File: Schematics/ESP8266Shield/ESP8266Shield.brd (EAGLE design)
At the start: 49.2 x 48.3 mm, 23 parts, among them IC1 MEGA8-P, Q1 2N5088, Q2 2N5088

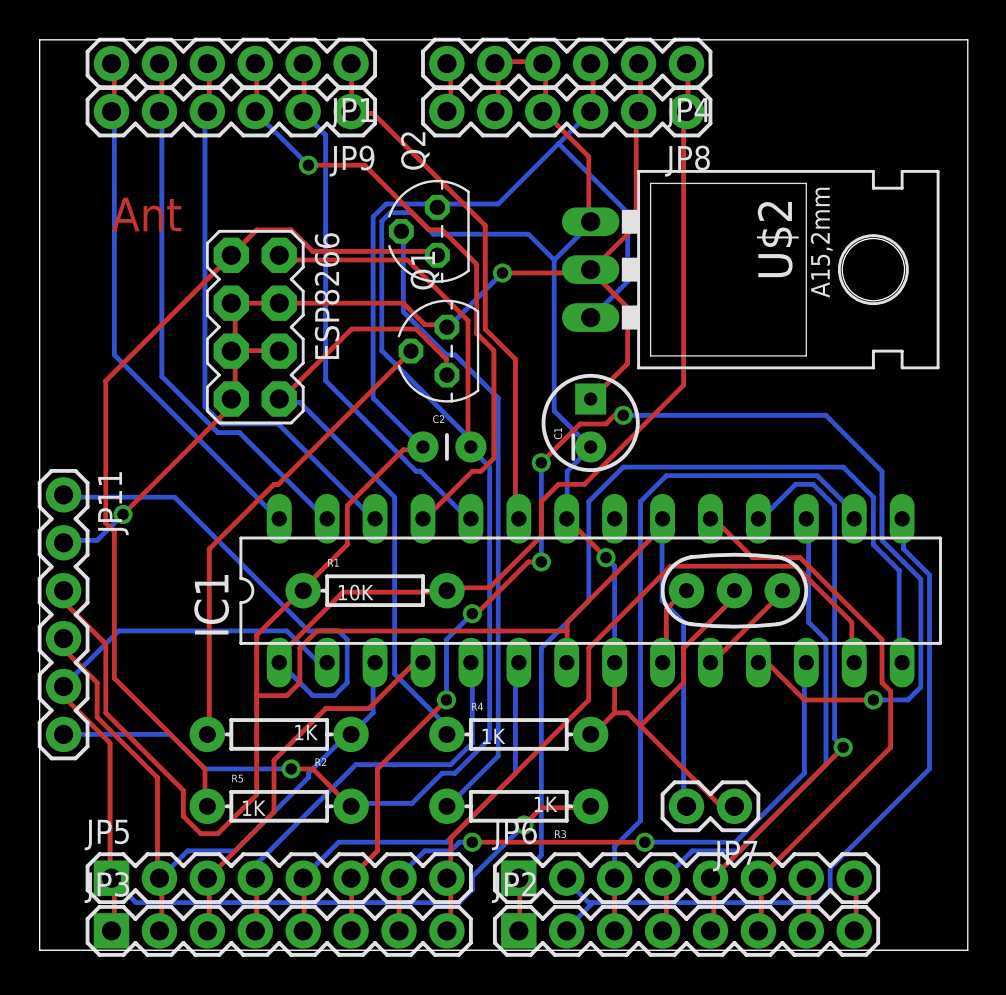
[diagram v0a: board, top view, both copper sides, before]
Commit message: v0.08
Updated Android project to close socket on exit
Updated Arduino projects
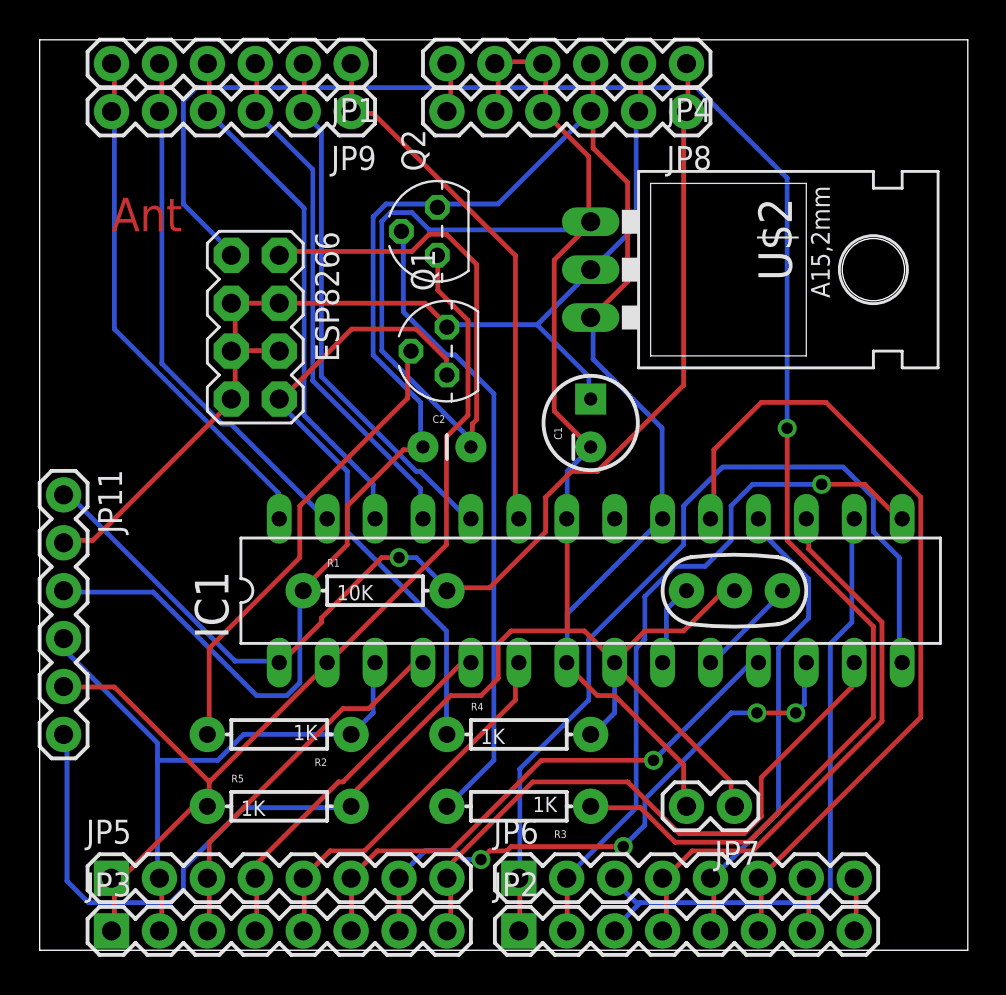
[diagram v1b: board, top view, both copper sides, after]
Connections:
- net D0: now also Q2.3, R5.P$1; no longer R3.P$1
- net ESPTX: now also R3.P$1; no longer Q2.3, R5.P$1
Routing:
- net ESPTX: track 46.2 -> 92.5 mm, vias 0 -> 1
- net D5: track 71.9 -> 29.2 mm, vias 6 -> 1
- net VCC: track 128.5 -> 106.2 mm
- net D13: track 30.4 -> 44.7 mm
- net RESET: track 71.1 -> 62.6 mm, vias 0 -> 1
- net GND: track 147.7 -> 154.8 mm, vias 2 -> 0
- net D12: track 31.1 -> 25.4 mm, vias 1 -> 0
- net D16: track 33.4 -> 27.9 mm, vias 1 -> 0
- net 3.3V: track 61.8 -> 58.1 mm, vias 2 -> 0
- net D7: track 37.6 -> 33.9 mm
- net D0: track 58.6 -> 55.0 mm, vias 1 -> 0
- net D8: track 50.2 -> 47.2 mm
- net D11: track 27.7 -> 30.5 mm
- net D1: track 35.5 -> 32.9 mm
- net D3: track 22.0 -> 19.4 mm
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
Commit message: V0.13
Updated ESP8266_Shield so that soft-serial can be used.
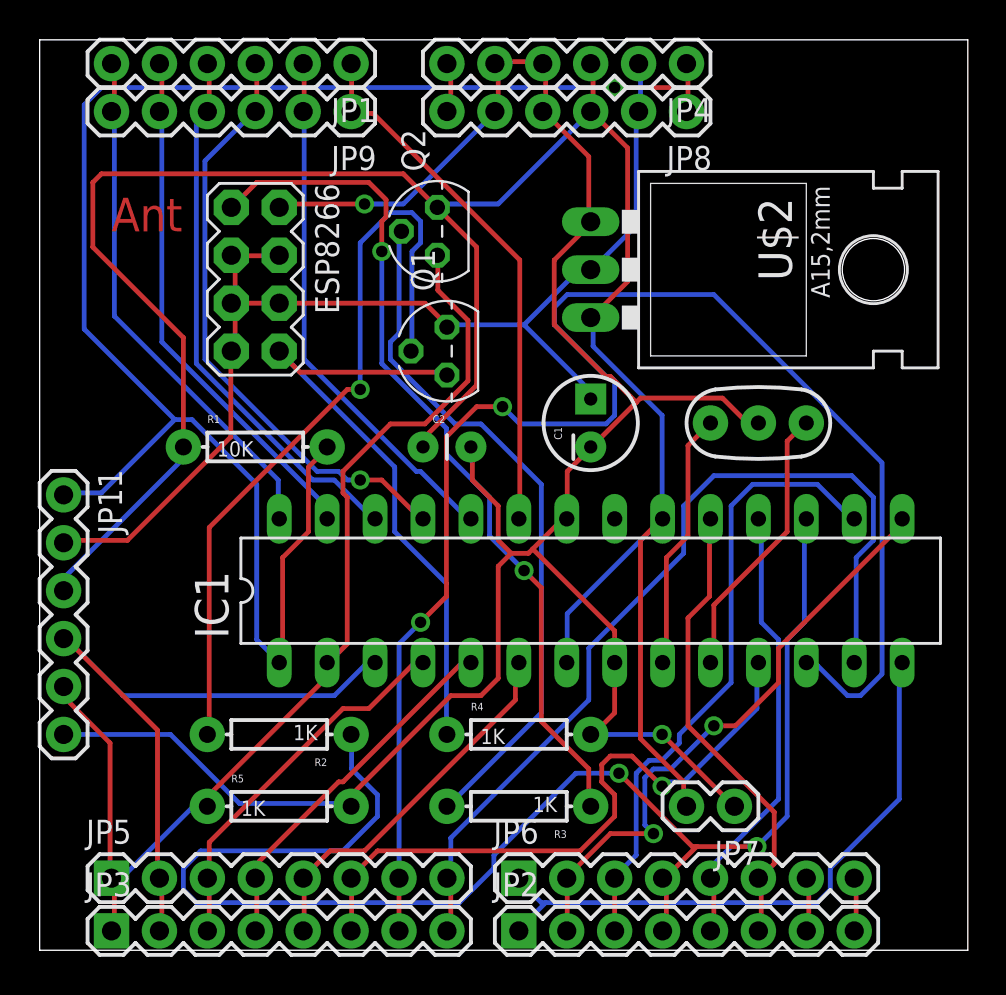
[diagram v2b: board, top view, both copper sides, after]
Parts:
- moved R1 9.92 mm to (38.1, 26.7)
- moved 16MHZ 8.98 mm to (64.8, 27.9)
- moved ESP8266 2.54 mm to (38.1, 35.6)
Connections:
- net D1: no longer R2.P$1
- net D11: now also R2.P$1
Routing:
- net D6: track 31.6 -> 82.3 mm, vias 4 -> 2
- net ESPTX: track 92.5 -> 46.0 mm, vias 1 -> 2
- net D11: track 30.5 -> 77.0 mm, vias 0 -> 2
- net GND: track 154.8 -> 122.0 mm, vias 0 -> 2
- net RESET: track 62.6 -> 89.4 mm
- net D13: track 44.7 -> 24.8 mm
- net VCC: track 106.2 -> 124.4 mm
- net N$3: track 24.8 -> 41.0 mm, vias 0 -> 1
- net D7: track 33.9 -> 48.4 mm
- net D8: track 47.2 -> 33.1 mm
- net N$1: track 5.45 -> 14.9 mm
- net N$2: track 4.42 -> 13.8 mm
- net D5: track 29.2 -> 34.4 mm
- net D9: track 37.4 -> 32.2 mm, vias 1 -> 2
- net D16: track 27.9 -> 31.9 mm, vias 0 -> 1
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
